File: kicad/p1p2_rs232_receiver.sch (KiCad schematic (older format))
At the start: 45 parts, among them J101 TE Connectivity 1776112-3, J102 Screw_Terminal_01x05, J103 Conn_01x03_Female, J104 Conn_01x03_Female, Q101 Q_NPN_BCE, U101 MAX22088, U102 ISO7342C, U103 ProMicro

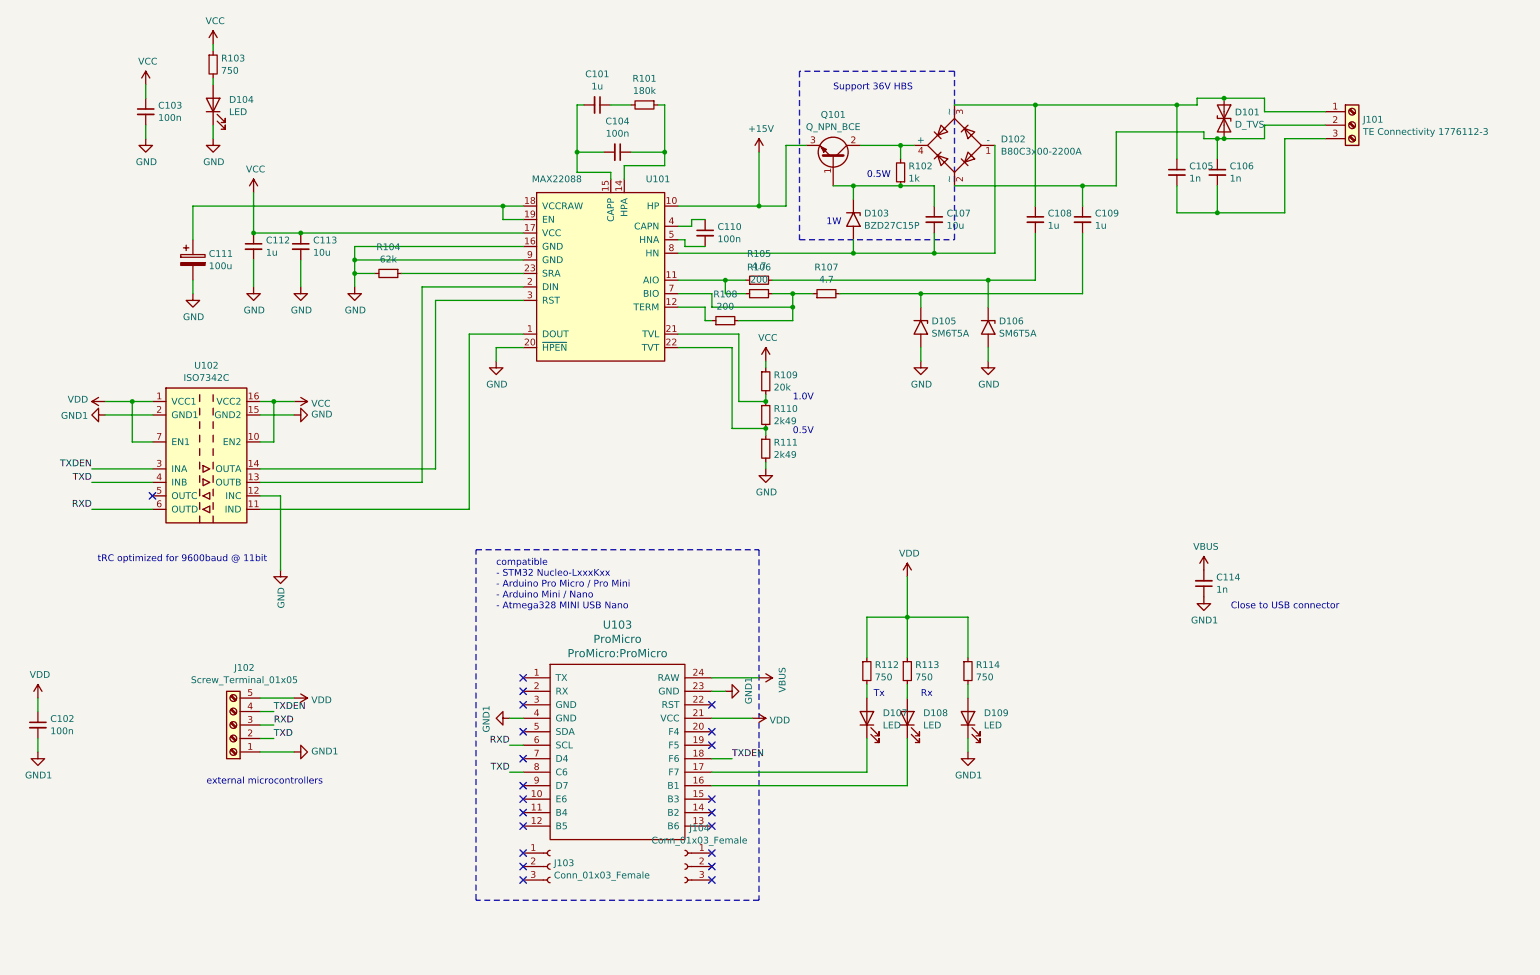
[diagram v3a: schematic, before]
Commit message: pcb: Convert to standalone AMI AFE
Signed-off-by: Patrick Rudolph <patrick.rudolph@9elements.com>
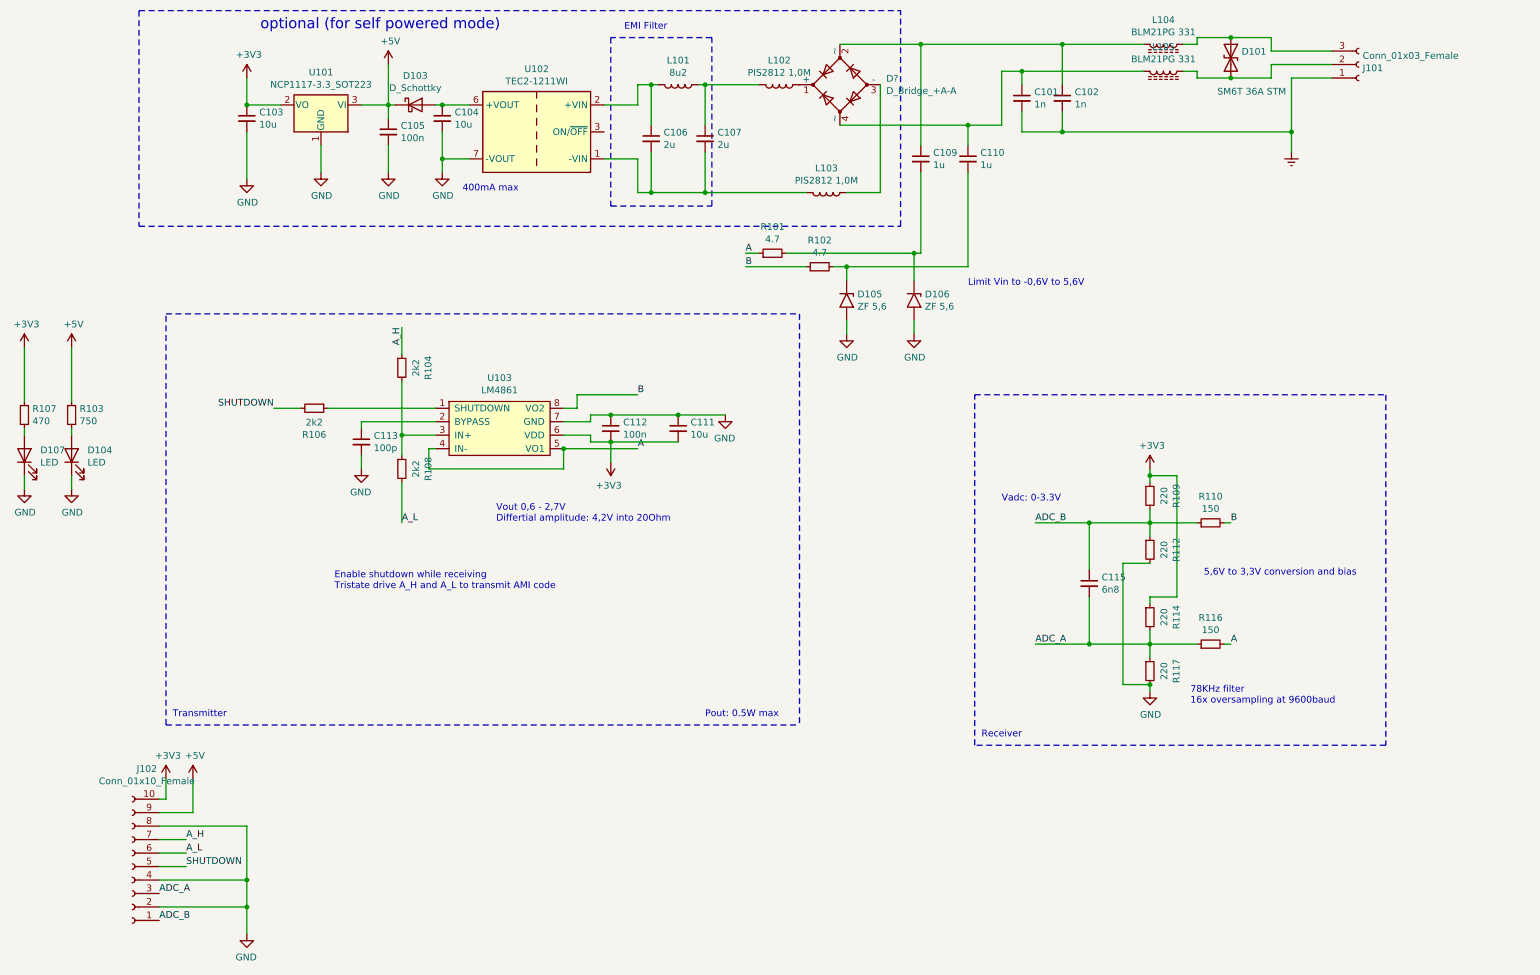
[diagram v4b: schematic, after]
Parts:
- removed C108: 1u, Capacitor_SMD:C_1206_3216Metric_Pad1.33x1.80mm_HandSolder, symbol Device:C_Small
- removed C111: 100u, Capacitor_THT:CP_Radial_D8.0mm_P5.00mm, symbol Device:CP
- removed C114: 1n, Capacitor_SMD:C_0805_2012Metric_Pad1.18x1.45mm_HandSolder, symbol Device:C_Small
- removed D102: B80C3x00-2200A, Diode_THT:Diode_Bridge_DIP-4_W7.62mm_P5.08mm, symbol Diode_Bridge:B80C3x00-2200A
- removed D103: BZD27C15P, Diode_SMD:D_SMF, symbol Diode:SM6T24A
- removed D108, D109: LED, LED_SMD:LED_0805_2012Metric_Pad1.15x1.40mm_HandSolder, symbol Device:LED
- removed J101: TE Connectivity 1776112-3, Connector_Wago:Wago_734-163_1x03_P3.50mm_Horizontal, symbol Connector:Screw_Terminal_01x03
- removed J102: Screw_Terminal_01x05, TerminalBlock_MetzConnect:TerminalBlock_MetzConnect_Type059_RT06305HBWC_1x05_P3.50mm_Horizontal, symbol Connector:Screw_Terminal_01x05
- removed J103, J104: Conn_01x03_Female, Connector_PinSocket_2.54mm:PinSocket_1x03_P2.54mm_Vertical, symbol Connector:Conn_01x03_Female
- removed Q101: Q_NPN_BCE, Package_TO_SOT_SMD:SOT-223-3_TabPin2, symbol Device:Q_NPN_BCE
- removed R105: 4.7, Resistor_SMD:R_1206_3216Metric_Pad1.30x1.75mm_HandSolder, symbol Device:R_Small
- removed R111: 2k49, Resistor_SMD:R_0805_2012Metric_Pad1.20x1.40mm_HandSolder, symbol Device:R_Small
- removed R113: 750, Resistor_SMD:R_0805_2012Metric_Pad1.20x1.40mm_HandSolder, symbol Device:R_Small
- removed U101: MAX22088, Package_DFN_QFN:QFN-24-1EP_4x4mm_P0.5mm_EP2.6x2.6mm, symbol MAX22088:MAX22088
- removed U102: ISO7342C, Package_SO:SOIC-16W_7.5x10.3mm_P1.27mm, symbol Isolator:ISO7342C
- removed U103: ProMicro, ProMicro:ProMicro, symbol ProMicro:ProMicro
- added C111: 10u, Capacitor_SMD:C_1210_3225Metric_Pad1.33x2.70mm_HandSolder, symbol Device:C_Small
- added C115: 6n8, Capacitor_SMD:C_0603_1608Metric_Pad1.08x0.95mm_HandSolder, symbol Device:C_Small
- added D103: D_Schottky, Diode_SMD:D_SMB, symbol Device:D_Schottky
- added D?: D_Bridge_+A-A, Diode_THT:Diode_Bridge_Round_D9.0mm, symbol Device:D_Bridge_+A-A
- added J101: Conn_01x03_Female, Connector_PinHeader_2.54mm:PinHeader_1x03_P2.54mm_Horizontal, symbol Connector:Conn_01x03_Female
- added J102: Conn_01x10_Female, Connector_PinSocket_2.54mm:PinSocket_1x10_P2.54mm_Horizontal, symbol Connector:Conn_01x10_Female
- added L101: 8u2, Inductor_SMD:L_1206_3216Metric_Pad1.42x1.75mm_HandSolder, symbol Device:L
- added L102, L103: PIS2812 1,0M, Inductor_SMD:L_7.3x7.3_H4.5, symbol Device:L
- added L104, L105: BLM21PG 331, Inductor_SMD:L_0805_2012Metric_Pad1.15x1.40mm_HandSolder, symbol Device:L_Core_Ferrite
- added R116: 150, Resistor_SMD:R_0805_2012Metric_Pad1.20x1.40mm_HandSolder, symbol Device:R_Small
- added R117: 220, Resistor_SMD:R_0805_2012Metric_Pad1.20x1.40mm_HandSolder, symbol Device:R_Small
- added U101: NCP1117-3.3_SOT223, Package_TO_SOT_SMD:SOT-223-3_TabPin2, symbol Regulator_Linear:NCP1117-3.3_SOT223
- added U102: TEC2-1211WI, Converter_DCDC:Converter_DCDC_TRACO_TMR-xxxx_THT, symbol Converter_DCDC:TEC2-1211WI
- added U103: LM4861, Package_SO:SOIC-8_3.9x4.9mm_P1.27mm, symbol LM4861:LM4861
- C101: value 1u -> 1n; footprint Capacitor_SMD:C_1210_3225Metric_Pad1.33x2.70mm_HandSolder -> Capacitor_SMD:C_0603_1608Metric_Pad1.08x0.95mm_HandSolder
- C102: value 100n -> 1n; footprint Capacitor_SMD:C_0805_2012Metric_Pad1.18x1.45mm_HandSolder -> Capacitor_SMD:C_0603_1608Metric_Pad1.08x0.95mm_HandSolder
- C103, C104: value 100n -> 10u; footprint Capacitor_SMD:C_0805_2012Metric_Pad1.18x1.45mm_HandSolder -> Capacitor_SMD:C_1206_3216Metric_Pad1.33x1.80mm_HandSolder
- C105: value 1n -> 100n
- C106: value 1n -> 2u; footprint Capacitor_SMD:C_0805_2012Metric_Pad1.18x1.45mm_HandSolder -> Capacitor_SMD:C_1206_3216Metric_Pad1.33x1.80mm_HandSolder
- C107: value 10u -> 2u; footprint Capacitor_SMD:C_1812_4532Metric_Pad1.57x3.40mm_HandSolder -> Capacitor_SMD:C_1206_3216Metric_Pad1.33x1.80mm_HandSolder
- C109: footprint Capacitor_SMD:C_1206_3216Metric_Pad1.33x1.80mm_HandSolder -> Capacitor_SMD:C_1210_3225Metric_Pad1.33x2.70mm_HandSolder
- C110: value 100n -> 1u; footprint Capacitor_SMD:C_0805_2012Metric_Pad1.18x1.45mm_HandSolder -> Capacitor_SMD:C_1210_3225Metric_Pad1.33x2.70mm_HandSolder
- C112: value 1u -> 100n; footprint Capacitor_SMD:C_1210_3225Metric_Pad1.33x2.70mm_HandSolder -> Capacitor_SMD:C_0805_2012Metric_Pad1.18x1.45mm_HandSolder
- C113: value 10u -> 100p; footprint Capacitor_SMD:C_1812_4532Metric_Pad1.57x3.40mm_HandSolder -> Capacitor_SMD:C_0603_1608Metric_Pad1.08x0.95mm_HandSolder
- D101: value D_TVS -> SM6T 36A STM
- D105, D106: value SM6T5A -> ZF 5,6; footprint Diode_SMD:D_SMB -> Diode_THT:D_A-405_P7.62mm_Horizontal
- R101: value 180k -> 4.7; footprint Resistor_SMD:R_0805_2012Metric_Pad1.20x1.40mm_HandSolder -> Resistor_SMD:R_1206_3216Metric_Pad1.30x1.75mm_HandSolder
- R102: value 1k -> 4.7
- R104: value 62k -> 2k2
- R106, R108: value 200 -> 2k2; footprint Resistor_SMD:R_1206_3216Metric_Pad1.30x1.75mm_HandSolder -> Resistor_SMD:R_0805_2012Metric_Pad1.20x1.40mm_HandSolder
- R107: value 4.7 -> 470; footprint Resistor_SMD:R_1206_3216Metric_Pad1.30x1.75mm_HandSolder -> Resistor_SMD:R_0805_2012Metric_Pad1.20x1.40mm_HandSolder
- R109: value 20k -> 220
- R110: value 2k49 -> 150
- R112, R114: value 750 -> 220
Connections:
- net GND1 is gone; now on net Earth: C102.2
- net GND: now also C104.2, C105.2, C112.1, D107.1 (K), R112.2, C111.1, J102.2 (Pin_2), J102.4 (Pin_4), J102.8 (Pin_8), R117.2, U101.1 (GND), U102.7 (-VOUT), U103.7 (GND); no longer C112.2, R104.2
- net at C107.2: now also C106.2, L103.2, U102.1 (-VIN)
- net at D101.1 (A1): now also J101.3 (Pin_3), L104.1; no longer C105.1
- net at R102.2: now also C110.2, D105.1 (A1)
- net SHUTDOWN: now reaches R106.2
- net SHUTDOWN: now also J102.5 (Pin_5)
- net at R108.1: now also R104.2, U103.3 (IN+)
- net at C104.1: now also D103.2 (A), U102.6 (+VOUT); no longer R101.1
- net Earth: now reaches C101.2
- net Earth: now also J101.1 (Pin_1); no longer C104.2
- net ADC_B: now reaches R109.2, R110.1
- net ADC_B: now also R112.1, C115.1, J102.1 (Pin_1)
- net B: now reaches R110.2
- net B: now also R102.1, U103.8 (VO2)
- net A_H: now reaches R104.1
- net A_H: now also J102.7 (Pin_7)
- net at C110.1: now also C101.1, D?.4 (~~), L105.2
- net at C107.1: now also L101.1, L102.2; no longer R102.1
- net at D106.1 (A1): now also C109.2, R101.2
- net ADC_A: now reaches R114.2
- net ADC_A: now also C115.2, J102.3 (Pin_3), R116.1, R117.1
- net at D107.2 (A): now also R107.2; no longer R112.2
- removed net VCC: C103.1, C112.1, C113.1, R103.1, R109.1
- removed net VDD: C102.1, R112.1, R114.1
- new net: D?.1 (+), L102.1
- new net: C102.1, C109.1, D?.2 (~~), L104.2
- new net: D?.3 (-), L103.1
- new net: D101.2 (A2), J101.2 (Pin_2), L105.1
- new net: C106.1, L101.2, U102.2 (+VIN)
- new net: R106.1, U103.1 (SHUTDOWN)
- new net: C113.1, U103.2 (BYPASS)
- new net +3V3: C103.1, C111.2, C112.2, J102.10 (Pin_10), R107.1, R109.1, R114.1, U101.2 (VO), U103.6 (VDD)
- new net +5V: C105.1, D103.1 (K), J102.9 (Pin_9), R103.1, U101.3 (VI)
- new net A: R101.1, R116.2, U103.4 (IN-), U103.5 (VO1)
- new net A_L: J102.6 (Pin_6), R108.2
- no-connect marks 22 -> 0
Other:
- note added: "400mA max"
- note added: "5,6V to 3,3V conversion and bias"
- note added: "78KHz filter\n16x oversampling at 9600baud"
- note added: "EMI Filter"
- note added: "Enable shutdown while receiving\nTristate drive A_H and A_L to transmit AMI code"
- note added: "Limit Vin to -0,6V to 5,6V"
- note added: "Pout: 0.5W max"
- note added: "Receiver"
- note added: "Transmitter"
- note added: "Vadc: 0-3.3V"
- note added: "Vout 0,6 - 2,7V\nDiffertial amplitude: 4,2V into 20Ohm"
- note added: "optional (for self powered mode)"
- note removed: "0.5V"
- note removed: "0.5W"
- note removed: "1.0V"
- note removed: "1W"
- note removed: "Close to USB connector"
- note removed: "Rx"
- note removed: "Support 36V HBS"
- note removed: "Tx"
- note removed: "compatible\n- STM32 Nucleo-LxxxKxx\n- Arduino Pro Micro / Pro Mini\n- Arduino Mini / Nano\n- Atmega328 MINI USB Nano"
- note removed: "external microcontrollers"
- note removed: "tRC optimized for 9600baud @ 11bit"
- moved on the sheet: D104, R103
